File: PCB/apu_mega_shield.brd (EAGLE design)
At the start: 105.4 x 53.6 mm, 36 parts, among them IC1 74HCT573D, IC2 4050D, IC3 DS1307, Q1 32.768, U1 IS62C1024AL-35QLI, X1 MICROSD

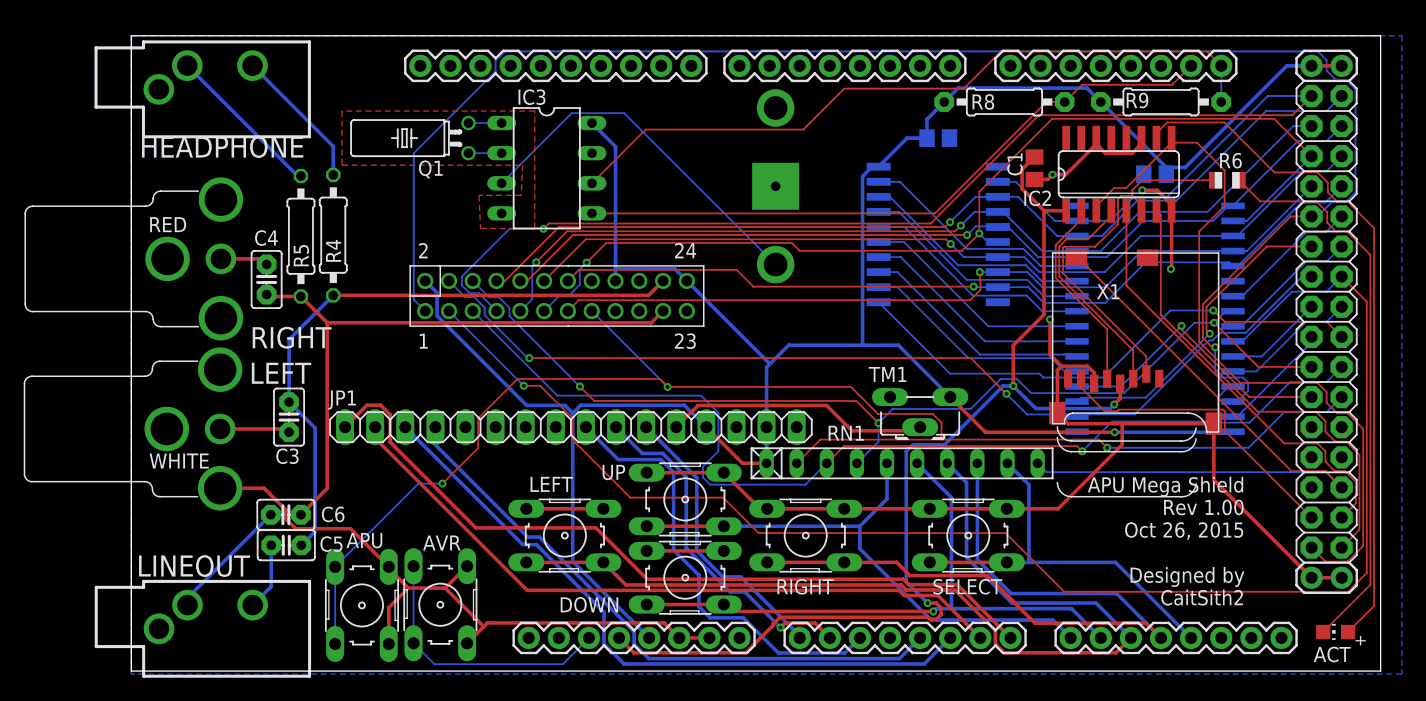
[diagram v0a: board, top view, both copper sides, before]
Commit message: Added 3.3v regulator due to Arduino 3.3v line being limited to 50ma. (Micro SD cards can draw up to 100ma while they are being written to.)
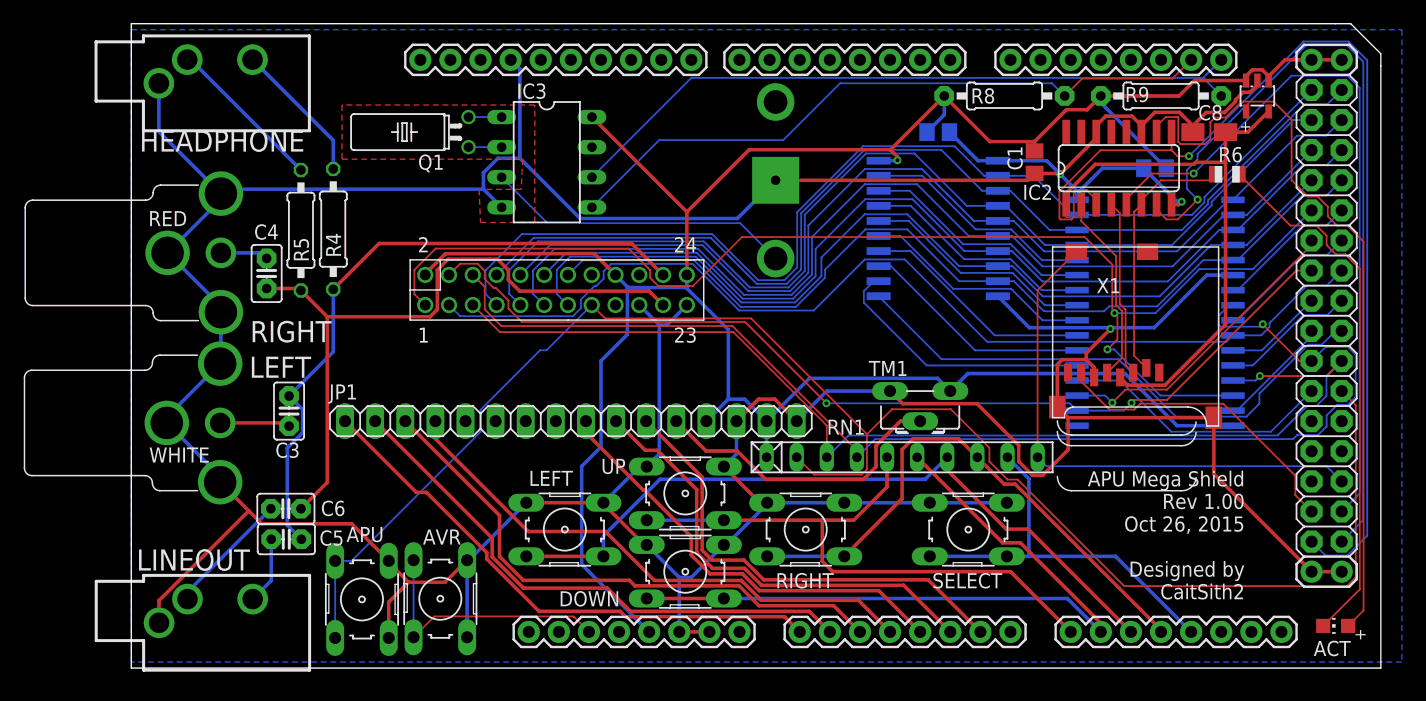
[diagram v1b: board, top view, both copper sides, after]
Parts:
- added C8: 10uF/10V, adafruit:A/3216-18R
- added IC4: LP298XS, adafruit:SOT23-5L
- moved BAT 0.51 mm to (54.4, 41.1)
- moved C2 0.51 mm to (86.4, 42.2)
- moved C4 0.51 mm to (11.4, 33.3)
- moved C7 0.51 mm to (68.1, 45.2)
- moved IC1 0.51 mm to (68.1, 37.1)
- moved IC2 0.51 mm to (83.3, 42.2)
- moved Q1 0.51 mm to (28.4, 45.2)
- moved R5 0.51 mm to (14.3, 36.9)
- moved RN1 0.51 mm to (65.0, 17.8)
- moved U1 0.51 mm to (86.4, 30.0)
- moved X1 0.51 mm to (77.7, 35.6)
- moved C6 0.51 mm to (13.0, 13.4)
- moved ACT 0.51 mm to (101.6, 3.56)
- moved APU 0.51 mm to (19.5, 5.79)
- moved AVR 0.51 mm to (26.1, 5.85)
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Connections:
- removed net N$14: JP1.11, U$6.A0
- removed net N$15: JP1.10, U$6.A1
- removed net N$16: JP1.9, U$6.A2
- removed net N$17: JP1.4, U$6.A4
- removed net N$18: JP1.3, U$6.A5
- removed net N$19: JP1.2, U$6.A6
- removed net N$20: JP1.1, U$6.A7
- new net LCD_D4: JP1.4, U$6.A3
- new net LCD_D5: JP1.3, U$6.A2
- new net LCD_D6: JP1.2, U$6.A1
- new net LCD_D7: JP1.1, U$6.A0
- new net LCD_E: JP1.9, U$6.A4
- new net LCD_R!W: JP1.10, U$6.A5
- new net LCD_RS: JP1.11, U$6.A6
- net +3V3: now also C8.+, IC4.5; no longer C1.1, U$6.3.3V
- net GND: now also C8.-, IC4.2
- net VCC: now also C1.1, IC4.1, IC4.3
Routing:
- net GND: track 180.9 -> 425.7 mm, vias 4 -> 3
- net N$20: track 66.4 -> 0.00 mm
- net N$19: track 59.0 -> 0.00 mm
- net N$18: track 56.7 -> 0.00 mm
- net N$17: track 51.2 -> 0.00 mm
- net LCD_D5: track 0.00 -> 47.7 mm
- net LCD_D6: track 0.00 -> 46.6 mm
- net LCD_D4: track 0.00 -> 46.6 mm
- net LCD_D7: track 0.00 -> 46.0 mm
- net +3V3: track 90.8 -> 47.4 mm, vias 3 -> 0
- net LCD_RS: track 0.00 -> 39.2 mm
- net A10: track 126.3 -> 87.3 mm, vias 1 -> 0
- net LCD_R!W: track 0.00 -> 38.7 mm
- net LCD_E: track 0.00 -> 37.0 mm
- net N$16: track 36.9 -> 0.00 mm
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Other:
- board size 105.4 x 53.6 mm -> 105.4 x 54.4 mm

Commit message: LCD now interfaced using 8-bit mode instead of 4-bit mode.
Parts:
- JP1: value (none) -> LCD
- RN1: value (none) -> 10K
- moved Q1 0.51 mm to (29.0, 45.2)
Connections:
- new net LCD_D0: JP1.8, U$6.A7
- new net LCD_D1: JP1.7, U$6.A6
- new net LCD_D2: JP1.6, U$6.A5
- new net LCD_D3: JP1.5, U$6.A4
- net DOWN: now also RN1.7, U$6.A13; no longer RN1.6, U$6.A9
- net LCD_E: now also U$6.A8; no longer U$6.A4
- net LCD_R!W: now also U$6.A9; no longer U$6.A5
- net LCD_RS: now also U$6.A10; no longer U$6.A6
- net LEFT: now also RN1.5, U$6.A11; no longer RN1.7, U$6.A10
- net RIGHT: now also U$6.A14; no longer U$6.A11
- net SELECT: now also U$6.A15; no longer U$6.A12
- net UP: now also RN1.6, U$6.A12; no longer RN1.5, U$6.A8
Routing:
- net LCD_D3: track 0.00 -> 49.3 mm
- net LCD_D2: track 0.00 -> 46.5 mm
- net LCD_D0: track 0.00 -> 46.5 mm
- net LCD_D1: track 0.00 -> 46.5 mm
- net LCD_E: track 37.0 -> 49.5 mm
- net LCD_R!W: track 38.7 -> 50.0 mm
- net LCD_RS: track 39.2 -> 48.3 mm
- net VCC: track 219.3 -> 211.2 mm
- net SELECT: track 33.8 -> 41.1 mm
- net RIGHT: track 46.6 -> 50.4 mm
- net UP: track 50.8 -> 54.2 mm
- net CS: track 69.1 -> 66.2 mm
- net DOWN: track 61.5 -> 59.5 mm
- net LEFT: track 62.2 -> 64.0 mm
- net RST: track 141.1 -> 142.0 mm
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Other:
- board text added: "APU Mega Shield Rev 1.00 Oct 29, 2015 Designed by CaitSith2"
- board text added: "D0"
- board text added: "D1"
- board text added: "D2"
- board text added: "D3"
- board text added: "D4"
- board text added: "D5"
- board text added: "D6"
- board text added: "D7"
- board text added: "E"
- board text added: "Gnd"
- board text added: "L+"
- board text added: "L-"
- board text added: "R!W"
- board text added: "RS"
- board text added: "Vcc"
- board text added: "v0"
- board text removed: "APU Mega Shield Rev 1.00 Oct 26, 2015 Designed by CaitSith2"

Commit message: Hopefully final PCB design for version 1.0 :)
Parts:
- added R1: 220, adafruit:0207/10
- IC1: value 74HCT573D -> 74AHC573
- U1: value IS62C1024AL-35QLI -> IS62C1024AL
- X1: value MICROSD -> MICROSDMOLEX; device adafruit:MICROSD -> adafruit:MICROSD-1
- moved X1 7.13 mm to (78.2, 28.4)
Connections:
- new net N$14: JP1.15, R1.2
- net CD: now also X1.11; no longer X1.CD1
- net GND: now also X1.12, X1.9; no longer X1.MT1, X1.MT2
- net VCC: now also R1.1; no longer JP1.15
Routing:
- net +3V3: track 47.4 -> 32.7 mm
- net CD: track 45.2 -> 58.1 mm
- net CLK: track 88.0 -> 77.2 mm
- net A15: track 106.5 -> 98.2 mm
- net N$7: track 22.0 -> 14.3 mm
- net N$12: track 14.9 -> 7.38 mm
- net N$14: track 0.00 -> 6.47 mm
- net DO: track 25.8 -> 31.2 mm
- net N$6: track 15.8 -> 12.1 mm
- net VCC: track 211.2 -> 214.6 mm
- net GND: track 425.4 -> 427.1 mm
- net A11: track 84.0 -> 82.8 mm
- net N$1: track 22.6 -> 21.5 mm
- net RST: track 142.0 -> 141.1 mm
- net A10: track 87.0 -> 87.6 mm
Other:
- board text added: "Micro SD"
